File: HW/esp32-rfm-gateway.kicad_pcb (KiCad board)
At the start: 2 copper layers, 99 x 93.5 mm, 56 parts, among them J1 Res, J2 Boot, J20 220V~, J21 c5V, J22 s14500, J23 s18650, J3 PinDbg, J30 AntSMA, J4 PinsI2C, J5 PinsI2C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

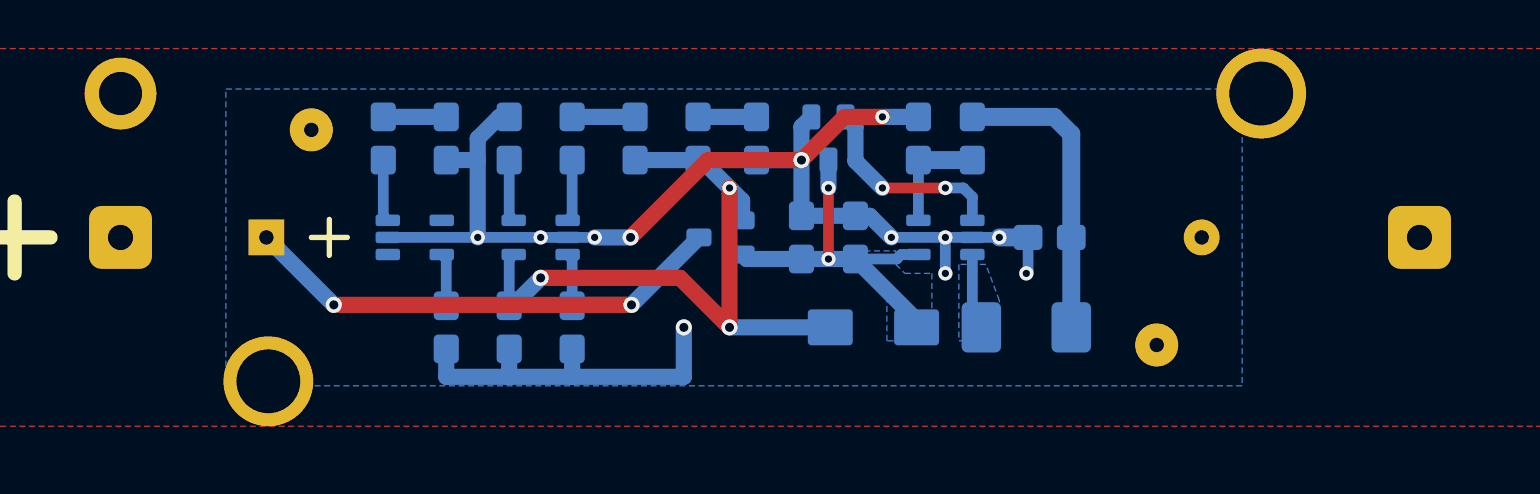
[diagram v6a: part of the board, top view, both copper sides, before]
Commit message: Adds a 3.3V header as placeholder in the power section
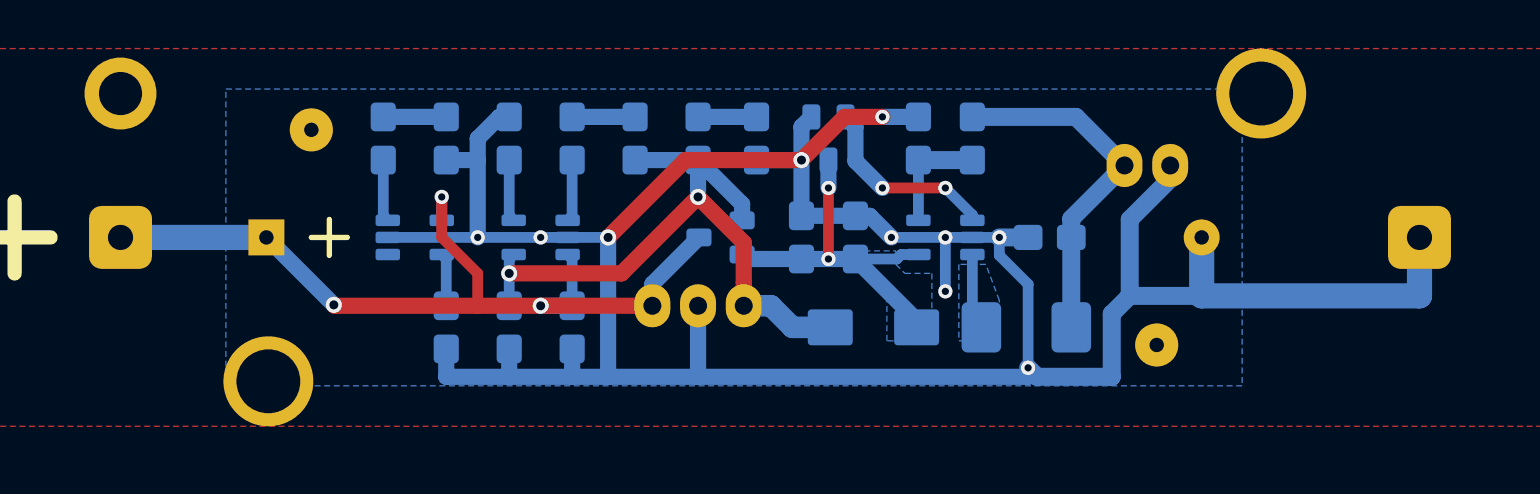
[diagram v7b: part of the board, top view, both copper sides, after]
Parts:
- added J24: cPS, CalinConnectors:Pin_Header_Angled_1x03, B.Cu at (76.0, 94.3)
- added J25: c3V3, CalinConnectors:Pin_Header_Angled_1x02, B.Cu at (104.8, 86.5)
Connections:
- J20 pad 2: Earth -> (no net)
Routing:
- net Earth: track 125.3 -> 0.00 mm, vias 17 -> 0
- net (no net): track 0.00 -> 125.3 mm, vias 0 -> 17
- net GND: track 87.7 -> 163.8 mm, vias 12 -> 10
- net +BATT: track 33.4 -> 48.9 mm, vias 2 -> 3
- net +3V3: track 16.6 -> 19.8 mm
- net +5VP: track 38.3 -> 37.5 mm, vias 3 -> 2
- net Net-(U22-Pad2): track 11.3 -> 10.7 mm

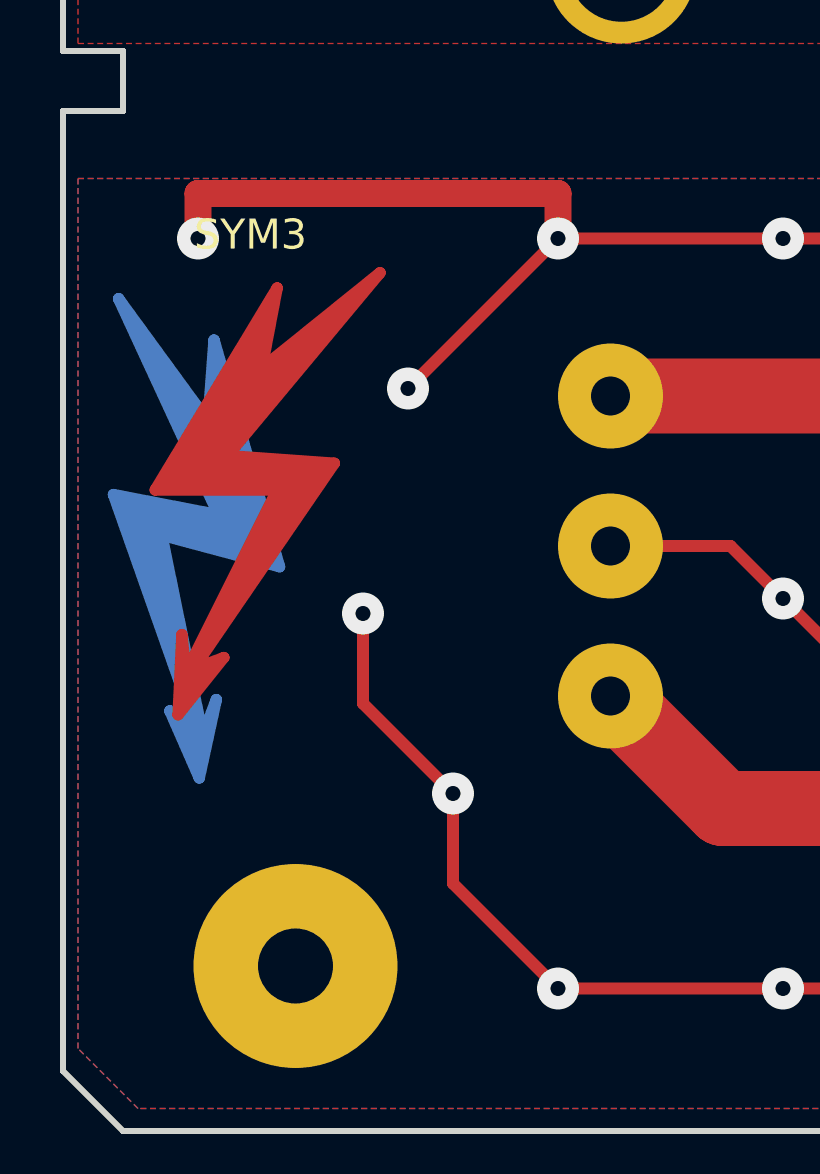
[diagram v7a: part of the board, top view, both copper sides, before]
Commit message: Adds an Earth screw hole and changes the High Voltage symbol
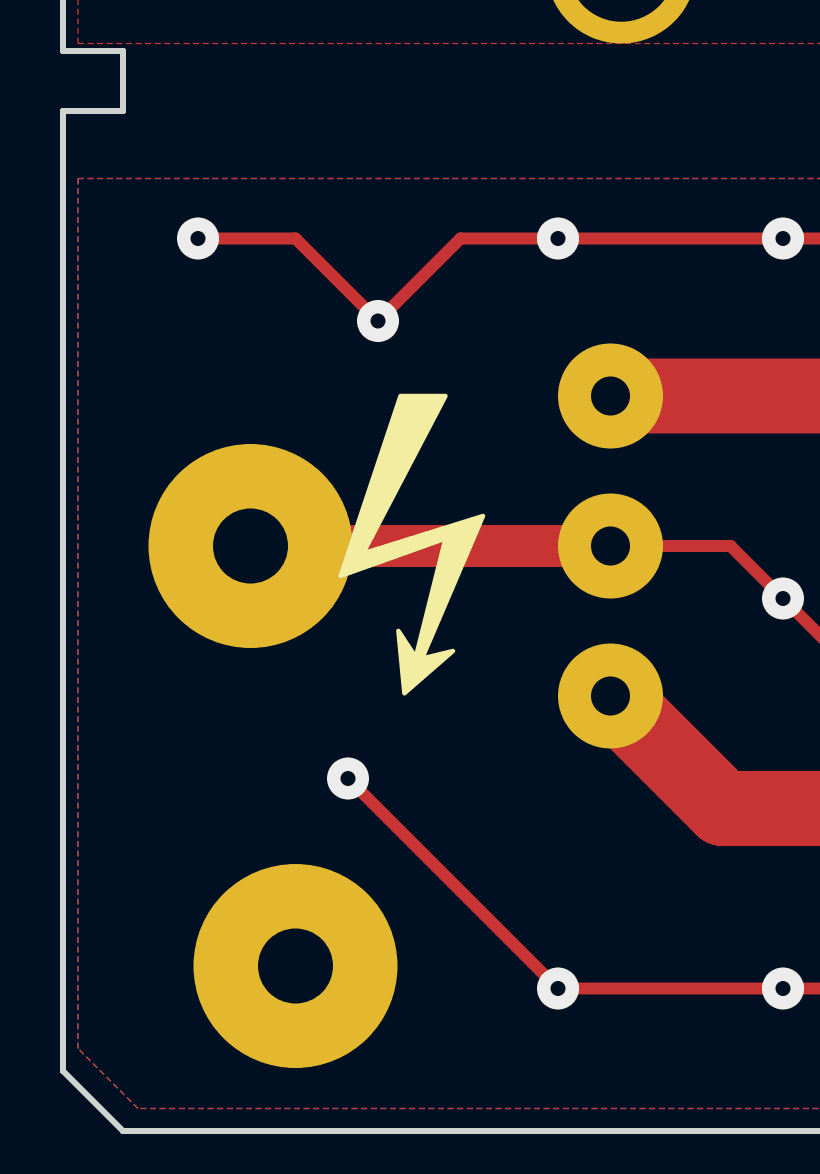
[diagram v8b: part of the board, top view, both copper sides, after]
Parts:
- added H5: HolePlated, CalinGeneric:HolePlated-M2.5, F.Cu at (42.2, 117.8)
- SYM3, SYM4: footprint Symbol:Symbol_HighVoltage_Type1_CopperTop_Big -> CalinGeneric:Symbol_HighVoltage_SilkS
- moved SYM4 8.02 mm to (48.2, 117.8), turned to 180 degrees
- moved SYM3 5.71 mm to (47.5, 117.8)
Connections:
- J20 pad 2: (no net) -> Earth
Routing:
- net (no net): track 125.3 -> 0.00 mm, vias 17 -> 0
- net Earth: track 0.00 -> 124.2 mm, vias 0 -> 16
